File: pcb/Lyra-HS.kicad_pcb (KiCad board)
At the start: 2 copper layers, 158.1 x 106.9 mm, 95 parts, among them J1 Computer/Power, J2 AVR-ISP-6, J3 AudioJack3, SW1 SW_Push, SW19 SW_Push, SW2 SW_Push, SW20 SW_Push, SW21 SW_Push, SW22 SW_Push, SW23 SW_Push, SW24 SW_Push, SW25 SW_Push, SW3 SW_Push, SW37 SW_Push, SW38 SW_Push, SW39 SW_Push, SW4 SW_Push, SW40 SW_Push, SW41 SW_Push, SW42 SW_Push, SW43 SW_Push, SW5 SW_Push, SW55 SW_Push, SW56 SW_Push, SW57 SW_Push, SW58 SW_Push, SW59 SW_Push, SW6 SW_Push, SW60 SW_Push, SW61 SW_Push, SW7 SW_Push, SW73 SW_Push, SW74 SW_Push, SW75 SW_Push, SW76 SW_Push, SW77 SW_Push, SW78 SW_Push, SW79 SW_Push, U1 ATmega32U4-MU, U2 SRV05-4, Y1 16mhz

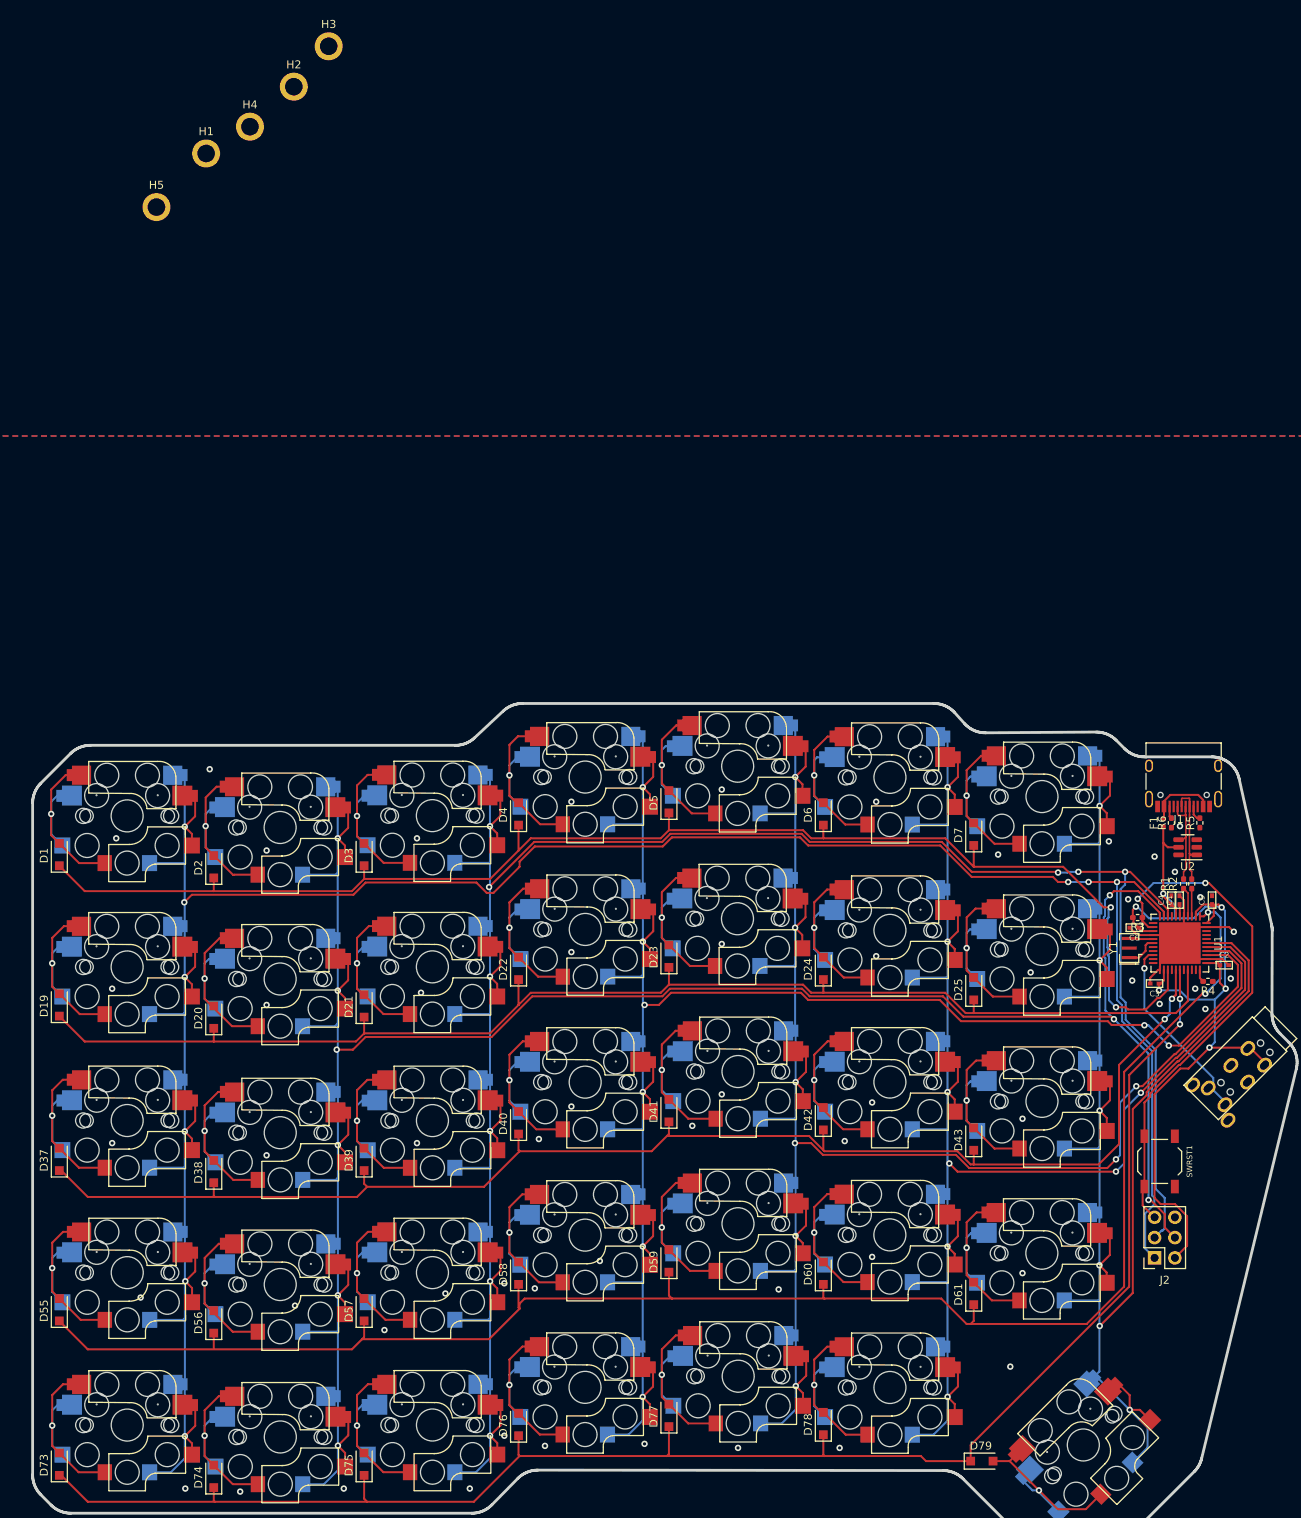
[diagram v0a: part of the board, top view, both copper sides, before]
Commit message: Matrix impedance optimisations
+change to desolder-friendly trrs jack footprint
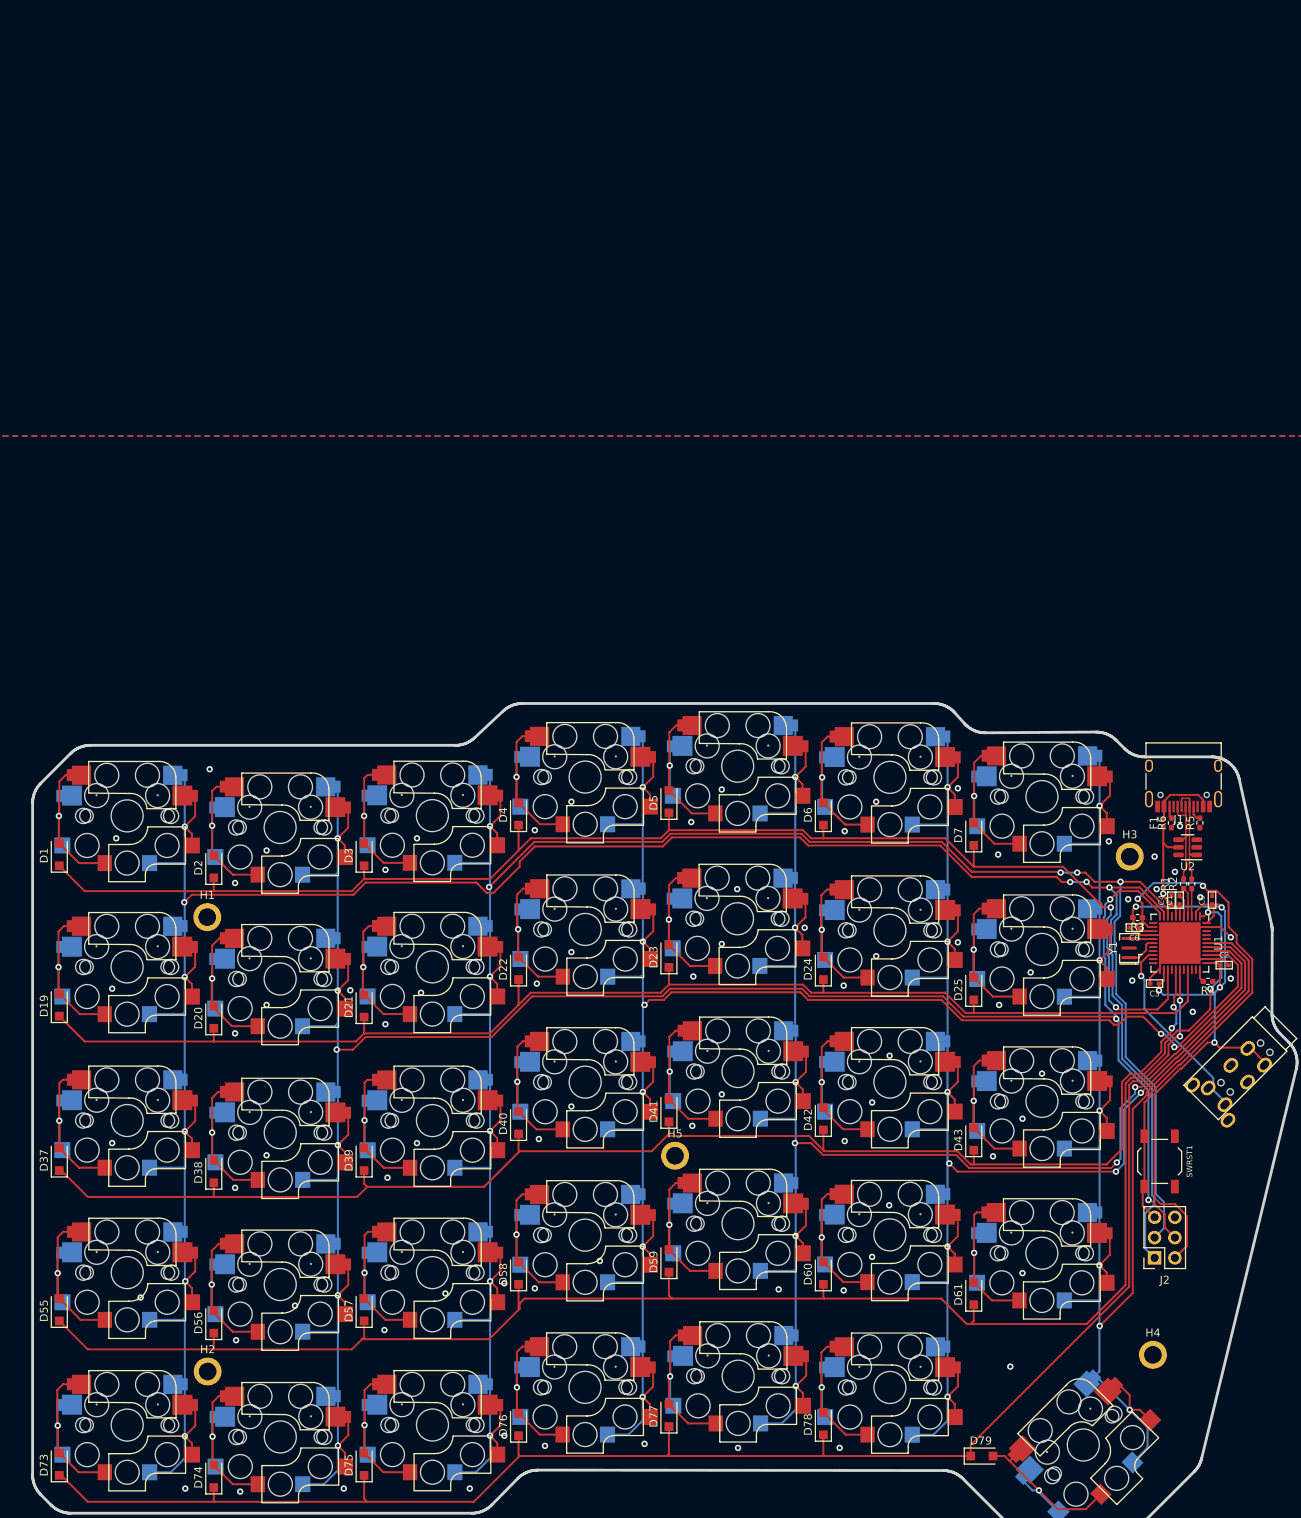
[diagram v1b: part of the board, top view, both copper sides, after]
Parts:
- moved H4 190.5 mm to (199.2, 127.1)
- moved H2 161.0 mm to (81.0, 129.1)
- moved H3 142.4 mm to (196.3, 64.8)
- moved H5 135.1 mm to (139.4, 102.2)
- moved H1 95.5 mm to (81.0, 72.3)
- moved D79 0.64 mm to (177.8, 139.7)
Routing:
- net VCC: track 117.4 -> 114.1 mm
- net Net-(D25-Pad2): track 24.7 -> 22.6 mm
- net Net-(D43-Pad2): track 24.5 -> 22.5 mm
- net Net-(D6-Pad2): track 24.1 -> 22.3 mm
- net Net-(D75-Pad2): track 24.3 -> 22.5 mm
- net Net-(D5-Pad2): track 24.2 -> 22.4 mm
- net Net-(D4-Pad2): track 24.1 -> 22.3 mm
- net Net-(D7-Pad2): track 24.1 -> 22.4 mm
- net Net-(D1-Pad2): track 24.2 -> 22.5 mm
- net Net-(D20-Pad2): track 23.8 -> 22.0 mm
- net Net-(D61-Pad2): track 24.5 -> 22.8 mm
- net Net-(D39-Pad2): track 24.4 -> 22.7 mm
- net Net-(D57-Pad2): track 24.3 -> 22.6 mm
- net Net-(D40-Pad2): track 24.2 -> 22.5 mm
- net Net-(D74-Pad2): track 23.9 -> 22.2 mm
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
